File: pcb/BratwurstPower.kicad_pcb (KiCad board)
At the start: 4 copper layers, 85 x 56 mm, 133 parts, among them J1 BarrelJack, J10 GPIO, J2 Raspi, J3 USB1in, J4 USB1out, J5 I2C, J6 I2C, J7 USB2in, J8 USB2out, J9 EXT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

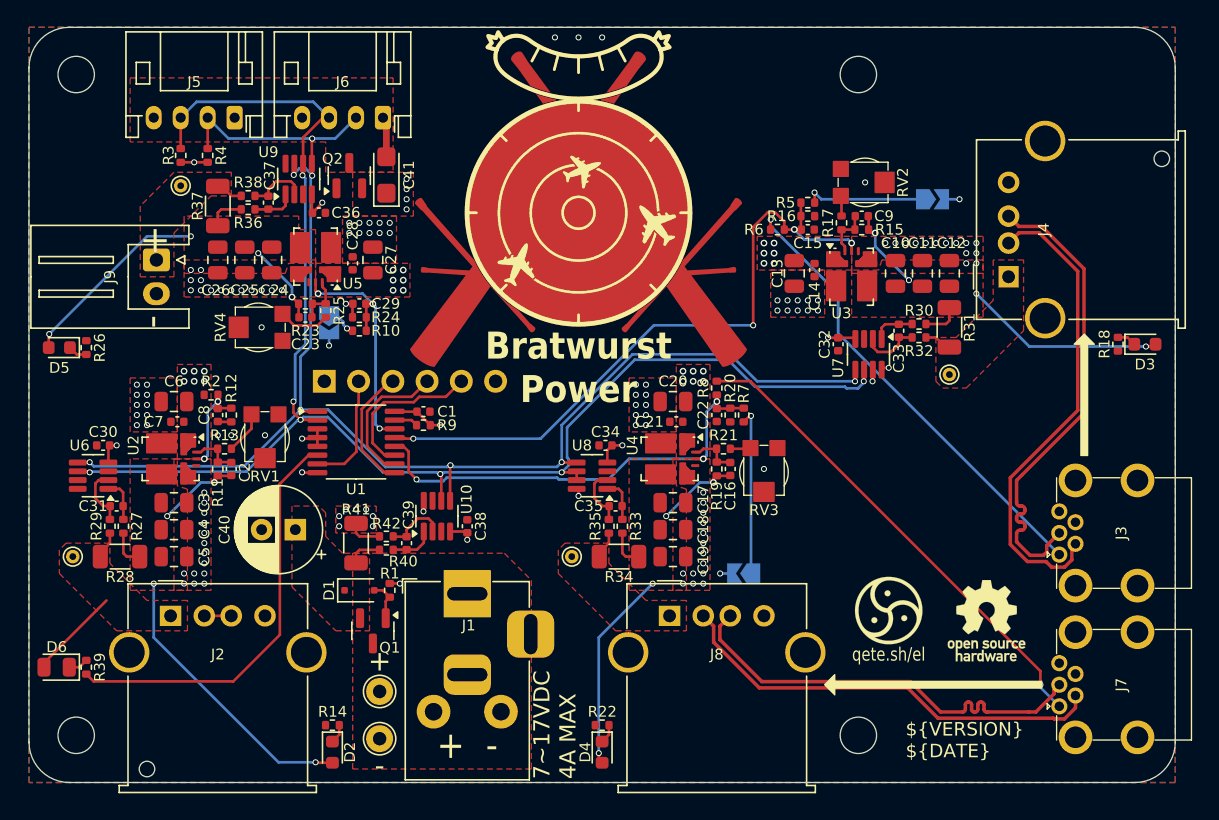
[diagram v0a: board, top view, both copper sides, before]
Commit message: fix: via stitching between GND layers
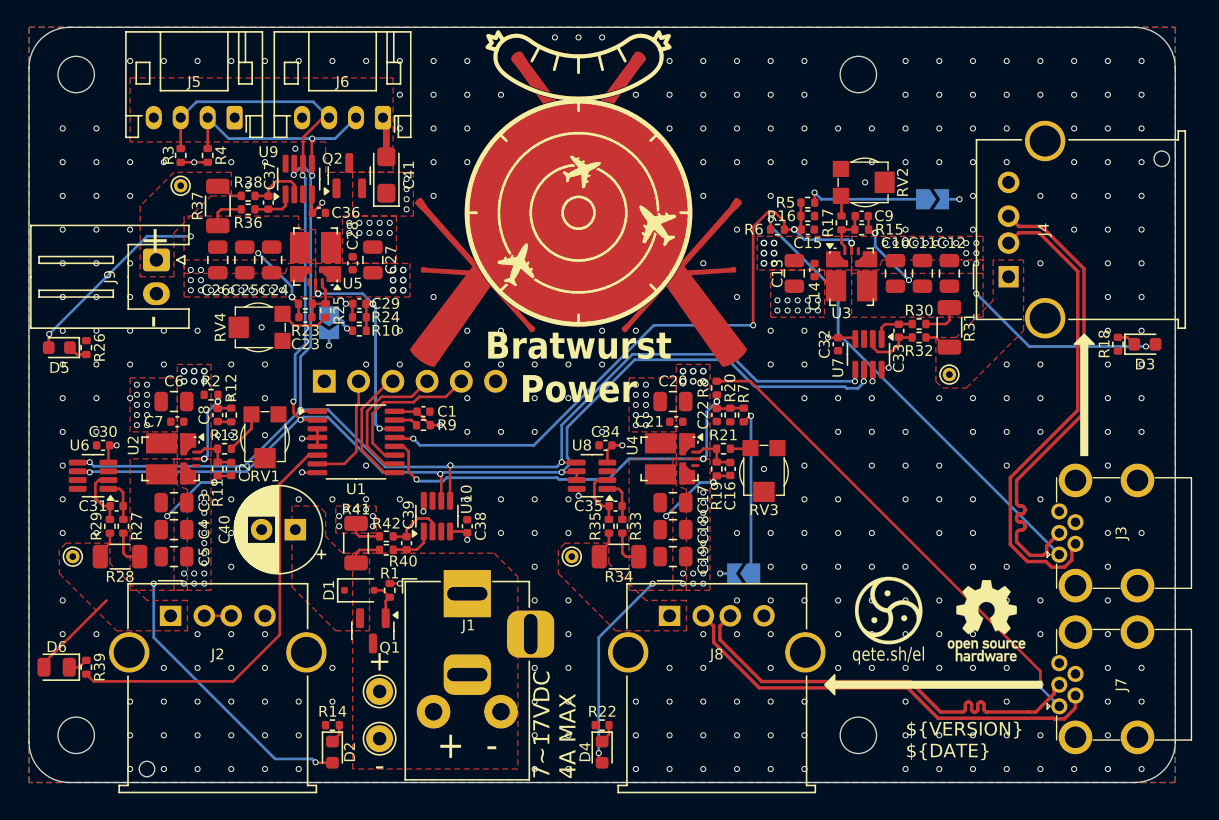
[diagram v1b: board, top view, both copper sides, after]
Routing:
- net GND: vias 110 -> 452

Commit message: fix: add clearance around USB traces
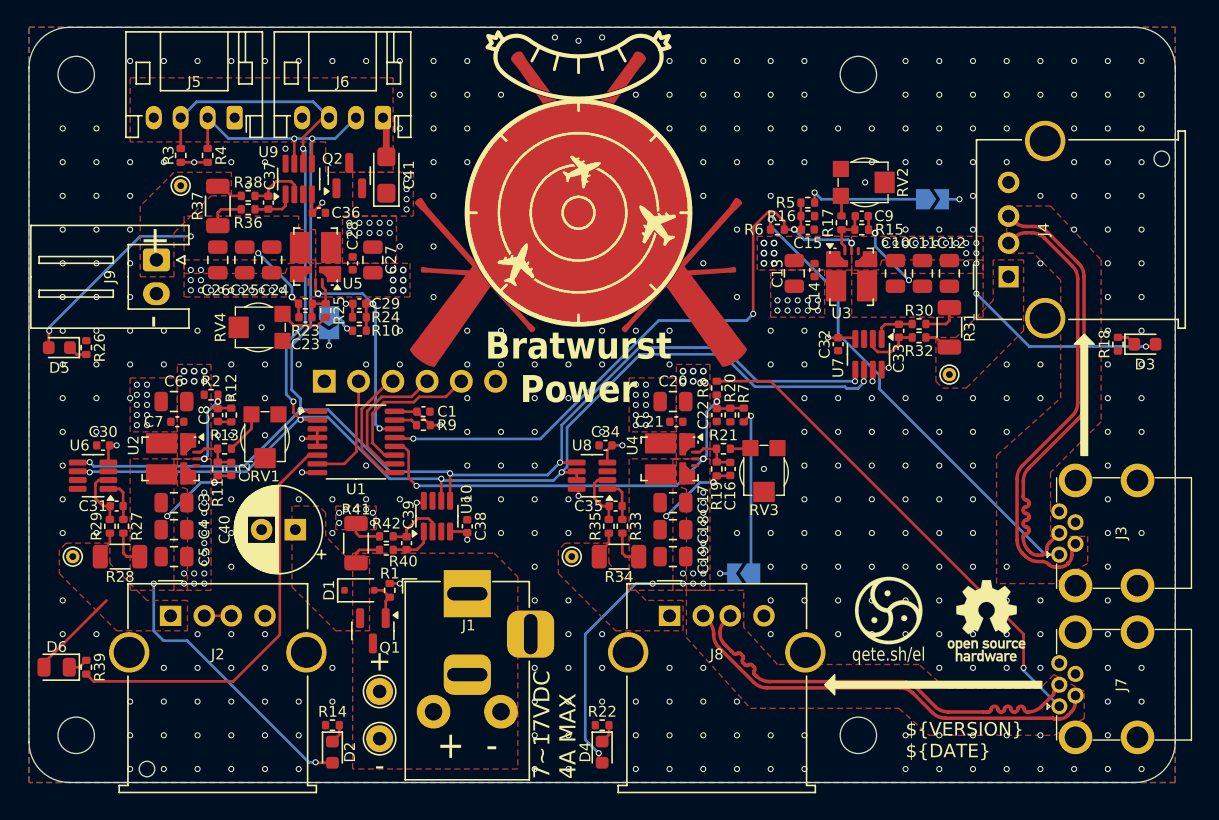
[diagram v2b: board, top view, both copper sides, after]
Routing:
- net SDA: track 112.6 -> 115.5 mm
- net SCL: track 111.0 -> 112.8 mm, vias 8 -> 7
- net /+5VBu2: track 24.0 -> 25.6 mm
- net /Du1-: track 35.7 -> 34.5 mm
- net /Du1+: track 35.6 -> 34.4 mm
- net /U1en: track 50.1 -> 49.2 mm
- net /U2vbus: track 36.1 -> 37.0 mm
- net /U1vbus: track 34.5 -> 35.1 mm
- net /Du2+: track 32.7 -> 32.1 mm
- net GND: vias 452 -> 461

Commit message: feat!: Replace USB mini and Raspi port with USB-C
feat: add connector for USB OTG connection
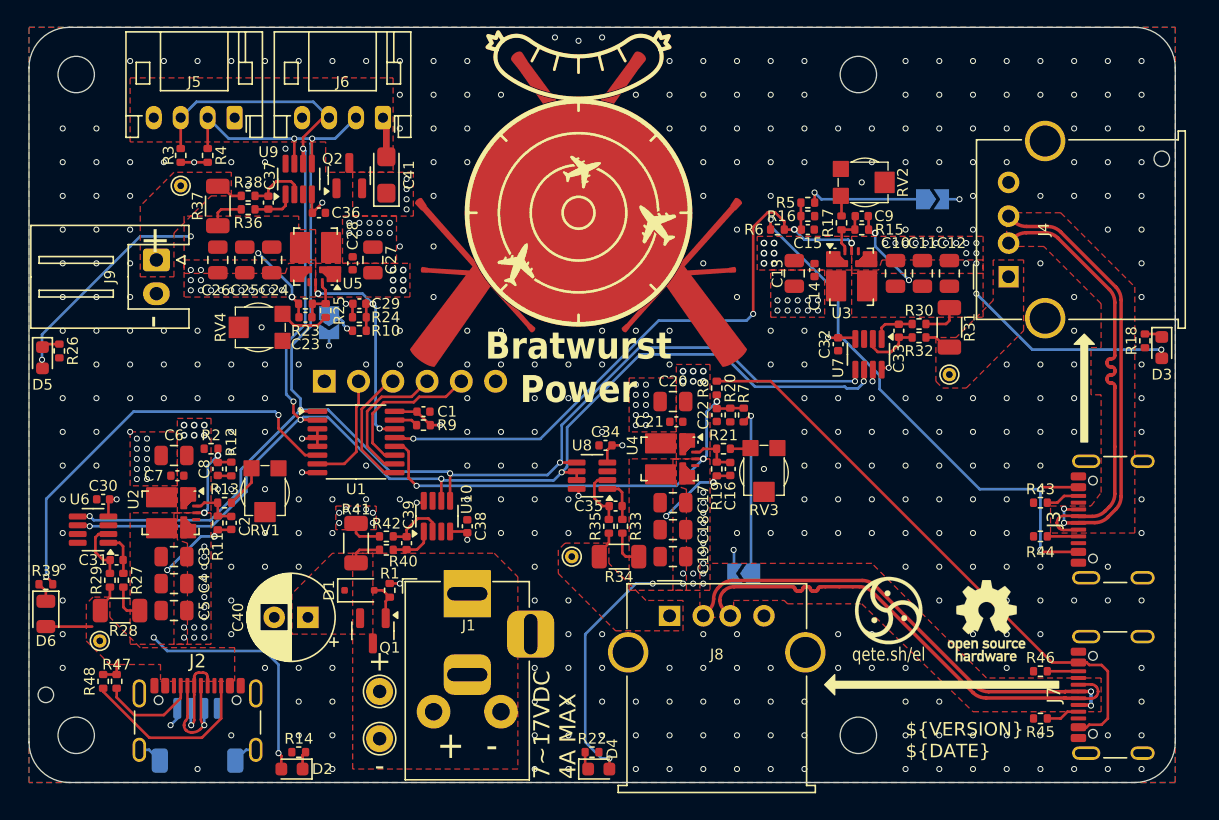
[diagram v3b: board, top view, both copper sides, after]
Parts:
- added J11: OTG, Connector_JST:JST_SH_SM04B-SRSS-TB_1x04-1MP_P1.00mm_Horizontal, B.Cu at (140.0, 132.5)
- added R43: 5k1, Resistor_SMD:R_0402_1005Metric, F.Cu at (202.5, 115.2)
- added R44: 5k1, Resistor_SMD:R_0402_1005Metric, F.Cu at (202.5, 117.8)
- added R45: 5k1, Resistor_SMD:R_0402_1005Metric, F.Cu at (202.5, 131.2)
- added R46: 5k1, Resistor_SMD:R_0402_1005Metric, F.Cu at (202.5, 127.8)
- added R47: 10k, Resistor_SMD:R_0402_1005Metric, F.Cu at (134.0, 128.5)
- added R48: 10k, Resistor_SMD:R_0402_1005Metric, F.Cu at (133.0, 128.5)
- J2: value Raspi -> RaspiPower; footprint Connector_USB:USB_A_Molex_67643_Horizontal -> Connector_USB:USB_C_Receptacle_GCT_USB4105-xx-A_16P_TopMnt_Horizontal
- J3, J7: footprint BratwurstPower:Connector_USB_Mini_THT -> Connector_USB:USB_C_Receptacle_GCT_USB4105-xx-A_16P_TopMnt_Horizontal
- moved REF** 9.30 mm to (128.8, 129.5)
- moved J2 9.08 mm to (140.0, 132.5)
- moved R39 6.84 mm to (128.8, 121.3), turned to 0 degrees
- moved C40 6.57 mm to (148.2, 123.8)
- moved TP1 6.56 mm to (132.8, 125.5)
- moved D6 4.03 mm to (128.8, 123.5), turned to -90 degrees
- moved C2 4.00 mm to (142.5, 116.8)
- moved C3 4.00 mm to (138.2, 119.2)
- moved C30 4.00 mm to (133.0, 115.0)
- moved C31 4.00 mm to (134.0, 119.5)
- moved C4 4.00 mm to (138.2, 121.2)
- moved C5 4.00 mm to (138.2, 123.2)
- moved C6 4.00 mm to (138.2, 111.8)
- moved C7 4.00 mm to (138.5, 113.2)
- moved C8 4.00 mm to (141.5, 112.8)
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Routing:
- net /CC2: track 0.00 -> 13.5 mm
- net /OTG_D-: track 0.00 -> 9.33 mm, vias 0 -> 1
- net /CC1: track 0.00 -> 7.46 mm
- net /U2vbus: track 37.0 -> 43.9 mm, vias 1 -> 0
- net /OTG_D+: track 0.00 -> 6.86 mm, vias 0 -> 1
- net /U1vbus: track 35.1 -> 41.8 mm, vias 1 -> 3
- net GND: track 8.70 -> 13.9 mm, vias 461 -> 454
- net /Du2+: track 32.1 -> 36.1 mm
- net /Du2-: track 32.3 -> 35.6 mm, vias 0 -> 2
- net /+5VBr: track 29.8 -> 26.9 mm
- net SDA: track 115.5 -> 118.0 mm
- net SCL: track 112.8 -> 115.3 mm
- net /USB2in/CC1: track 0.00 -> 2.47 mm
- net /USB1in/CC2: track 0.00 -> 2.47 mm
- net /USB2in/CC2: track 0.00 -> 2.27 mm
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
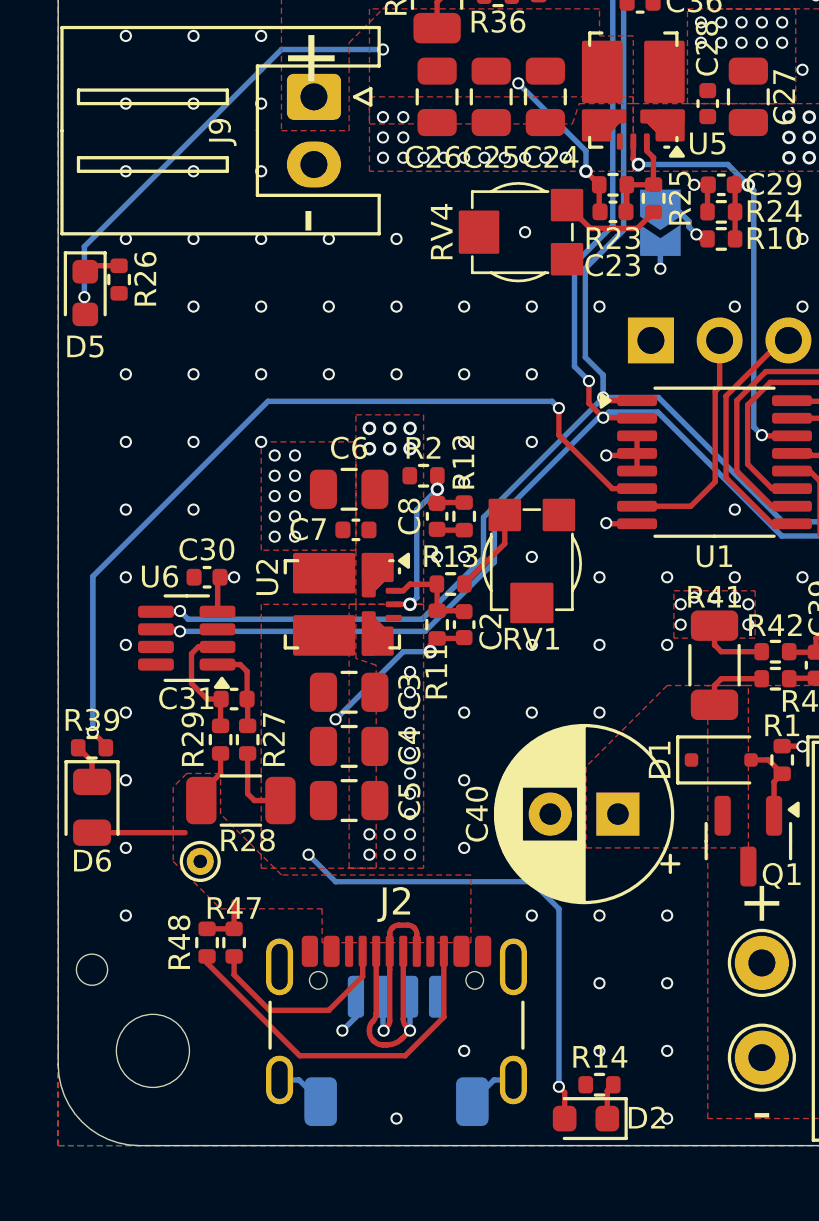
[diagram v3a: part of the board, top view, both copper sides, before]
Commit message: style: replace OTG connector
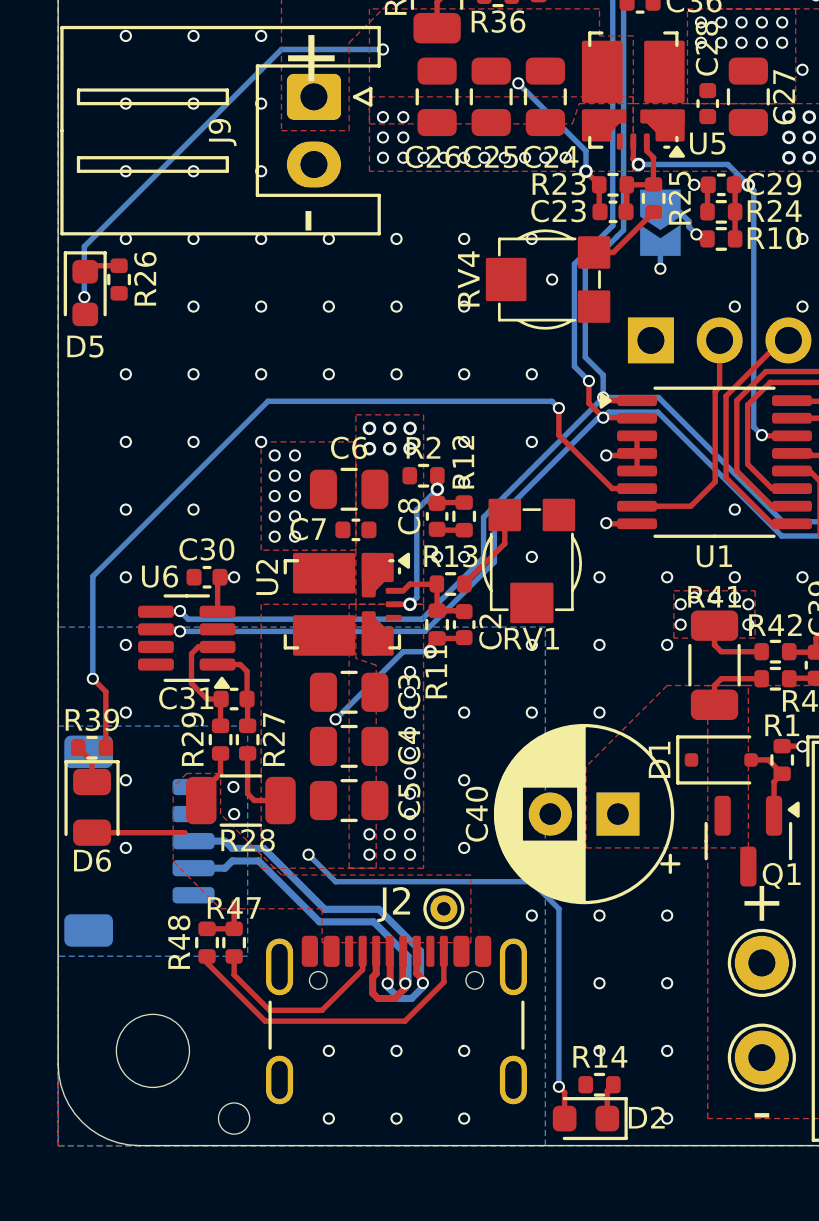
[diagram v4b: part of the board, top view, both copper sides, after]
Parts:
- J11: footprint Connector_JST:JST_SH_SM04B-SRSS-TB_1x04-1MP_P1.00mm_Horizontal -> Connector_JST:JST_SH_SM05B-SRSS-TB_1x05-1MP_P1.00mm_Horizontal
- moved J11 12.3 mm to (130.5, 124.8), turned to 90 degrees
- moved TP1 9.17 mm to (141.8, 127.2)
- moved REF** 7.60 mm to (134.0, 135.0)
- moved RV4 2.02 mm to (145.5, 104.0)
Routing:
- net /OTG_D+: track 6.86 -> 15.7 mm, vias 1 -> 2
- net /OTG_D-: track 9.33 -> 15.0 mm
- net GND: track 13.9 -> 8.70 mm, vias 454 -> 458
- net /CC2: track 13.5 -> 11.7 mm
- net /BuckEXT/FBt: track 3.88 -> 2.82 mm
- added copper zone on B.Cu, net GND
- added copper zone on In2.Cu, net GND
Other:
- board text added: "G G D+ D- VB"
